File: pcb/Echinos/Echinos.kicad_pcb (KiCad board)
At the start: 2 copper layers, 167 x 135.4 mm, 88 parts, among them J1 Conn_01x06_Socket, J2 Conn_01x06_Socket, J3 Conn_01x06_Socket, J5 SATA-7p, SW1 Reset, SW111 SW_Push, SW112 SW_Push, SW113 SW_Push, SW114 SW_Push, SW115 SW_Push, SW122 SW_Push, SW123 SW_Push, SW124 SW_Push, SW125 SW_Push, SW131 SW_Push, SW132 SW_Push, SW133 SW_Push, SW134 SW_Push, SW135 SW_Push, SW141 SW_Push, SW142 SW_Push, SW143 SW_Push, SW144 SW_Push, SW145 SW_Push, SW151 SW_Push, SW152 SW_Push, SW153 SW_Push, SW154 SW_Push, SW155 SW_Push, U1 Helios, U7 SRV05-4

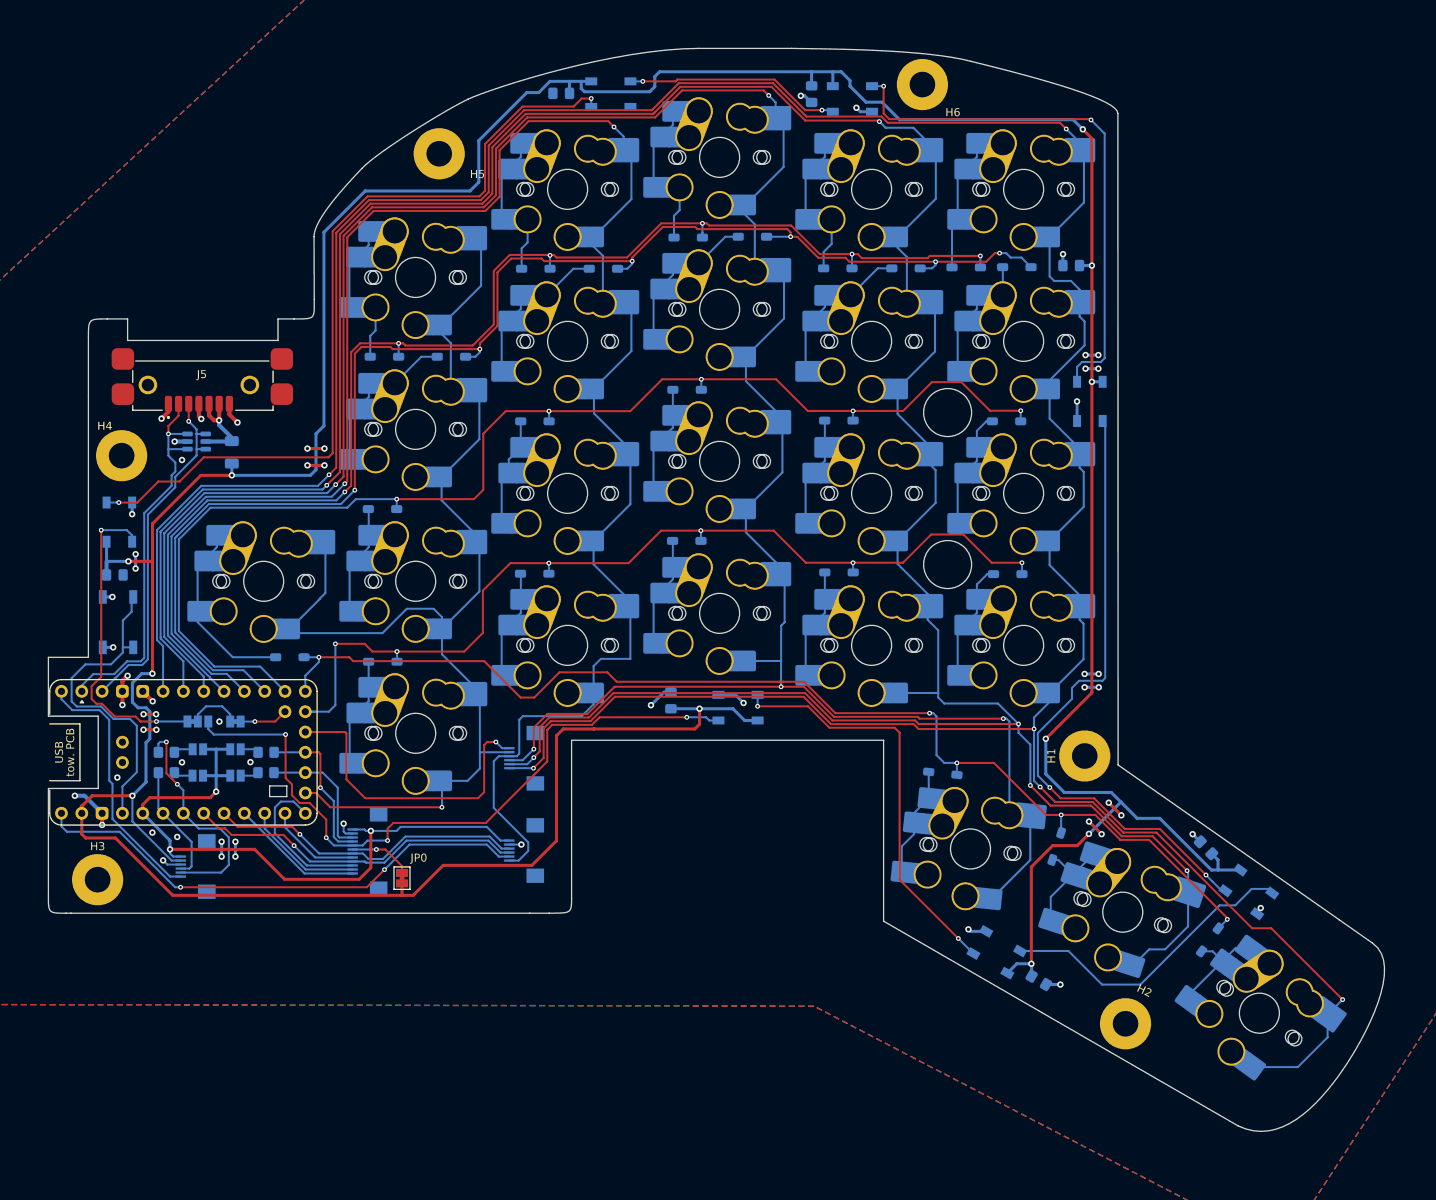
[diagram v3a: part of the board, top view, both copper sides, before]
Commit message: [PCB] - Save last state with Helios MCU board. Add multiple choices for split communication. Also fix SATA footprint and rework board (helios) holes to be smaller (0.9 --> 0.825) to be able to use spring loaded pins. Currently supported split communication are:   - SATA (data)   - USB-B (micro)   - Direct wires to whatever using 2.0 pitch header
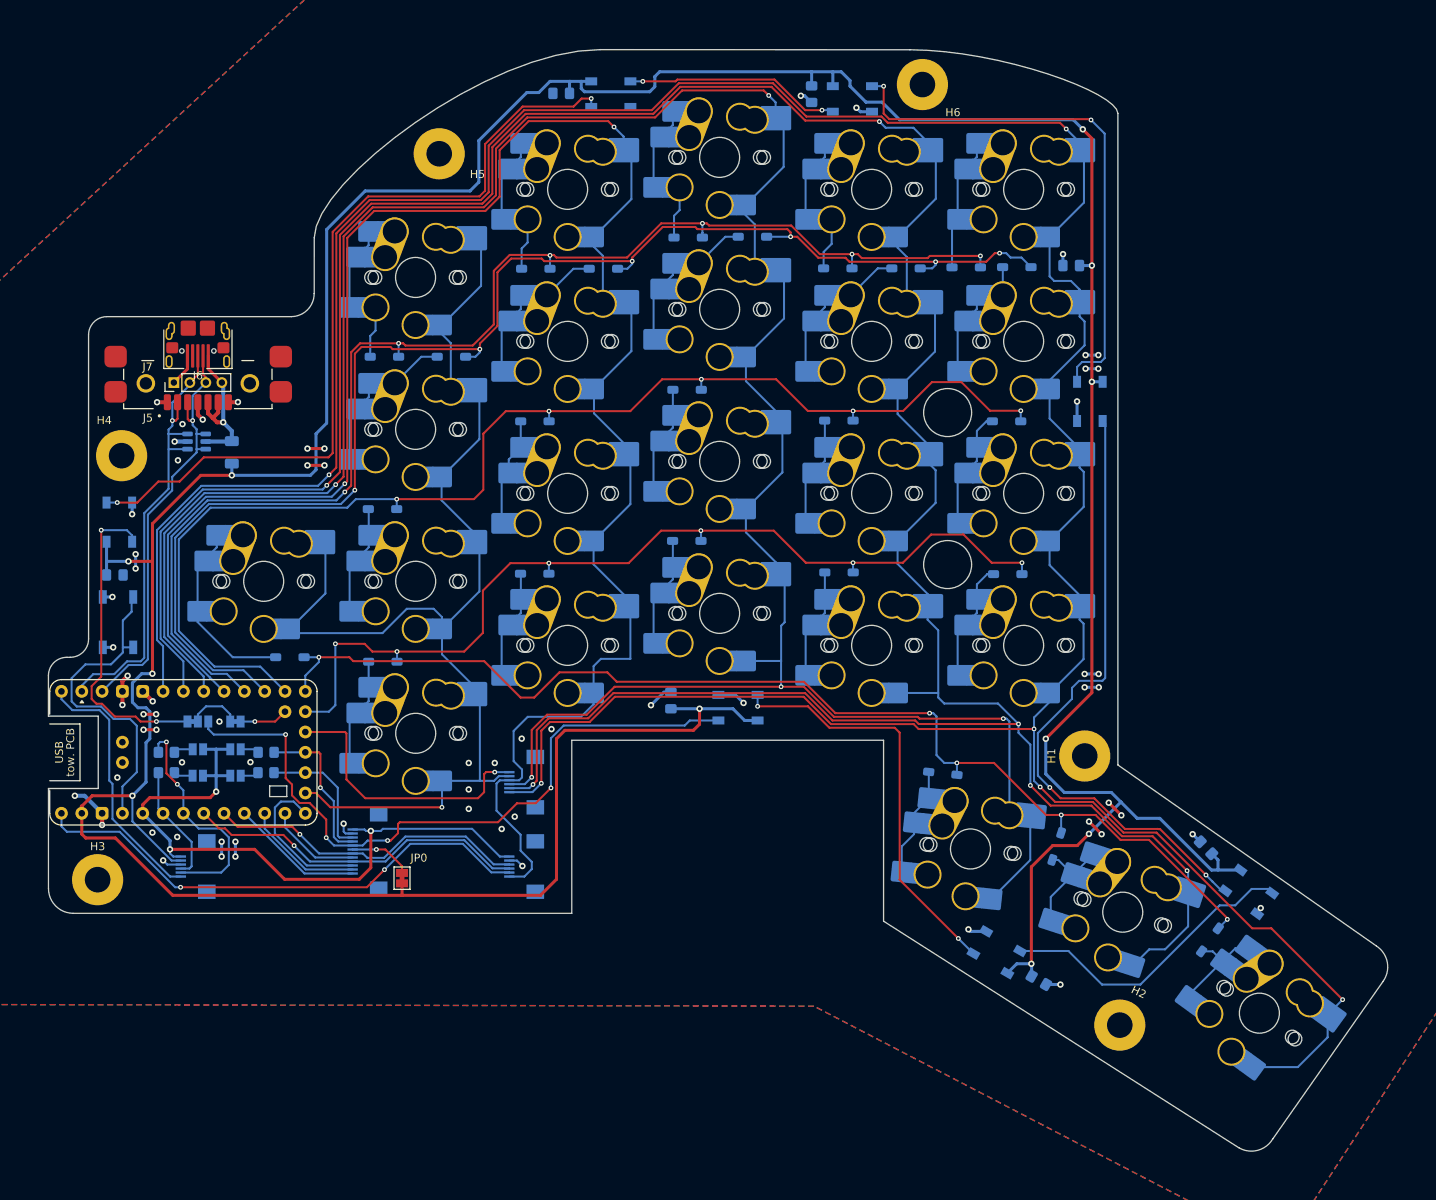
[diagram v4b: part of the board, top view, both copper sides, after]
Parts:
- added J6: USB_B_Micro, Echinos:USB_Micro-B_type5_Amphenol_Horizontal, F.Cu at (64.8, 82.9)
- added J7: Conn_01x04_Socket, Connector_PinHeader_2.00mm:PinHeader_1x04_P2.00mm_Vertical, F.Cu at (61.8, 88.6)
- moved J1 2.99 mm to (105.6, 138.5)
- moved J2 2.00 mm to (105.6, 149.1)
- moved H2 0.74 mm to (180.0, 168.9)
- moved J5 0.66 mm to (64.8, 88.7)
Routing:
- net VBUS_split: track 11.6 -> 21.2 mm
- net RX: track 44.5 -> 54.0 mm
- net TX: track 49.2 -> 58.3 mm
- net row6: track 39.0 -> 35.0 mm
- net col4: track 381.1 -> 384.2 mm
- net col3: track 328.1 -> 331.2 mm
- net col2: track 242.8 -> 245.8 mm
- net col5: track 416.6 -> 419.4 mm
- net GND: track 75.5 -> 78.0 mm, vias 58 -> 67
- net row2: track 119.6 -> 118.4 mm
- net col1: track 143.2 -> 144.3 mm
- net row7: track 63.6 -> 64.5 mm
- net +5V: track 506.1 -> 507.0 mm
- net rgb_out: track 85.9 -> 86.7 mm
- net adc_1: track 42.5 -> 43.3 mm
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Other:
- board size 167 x 135.4 mm -> 167.4 x 137.7 mm

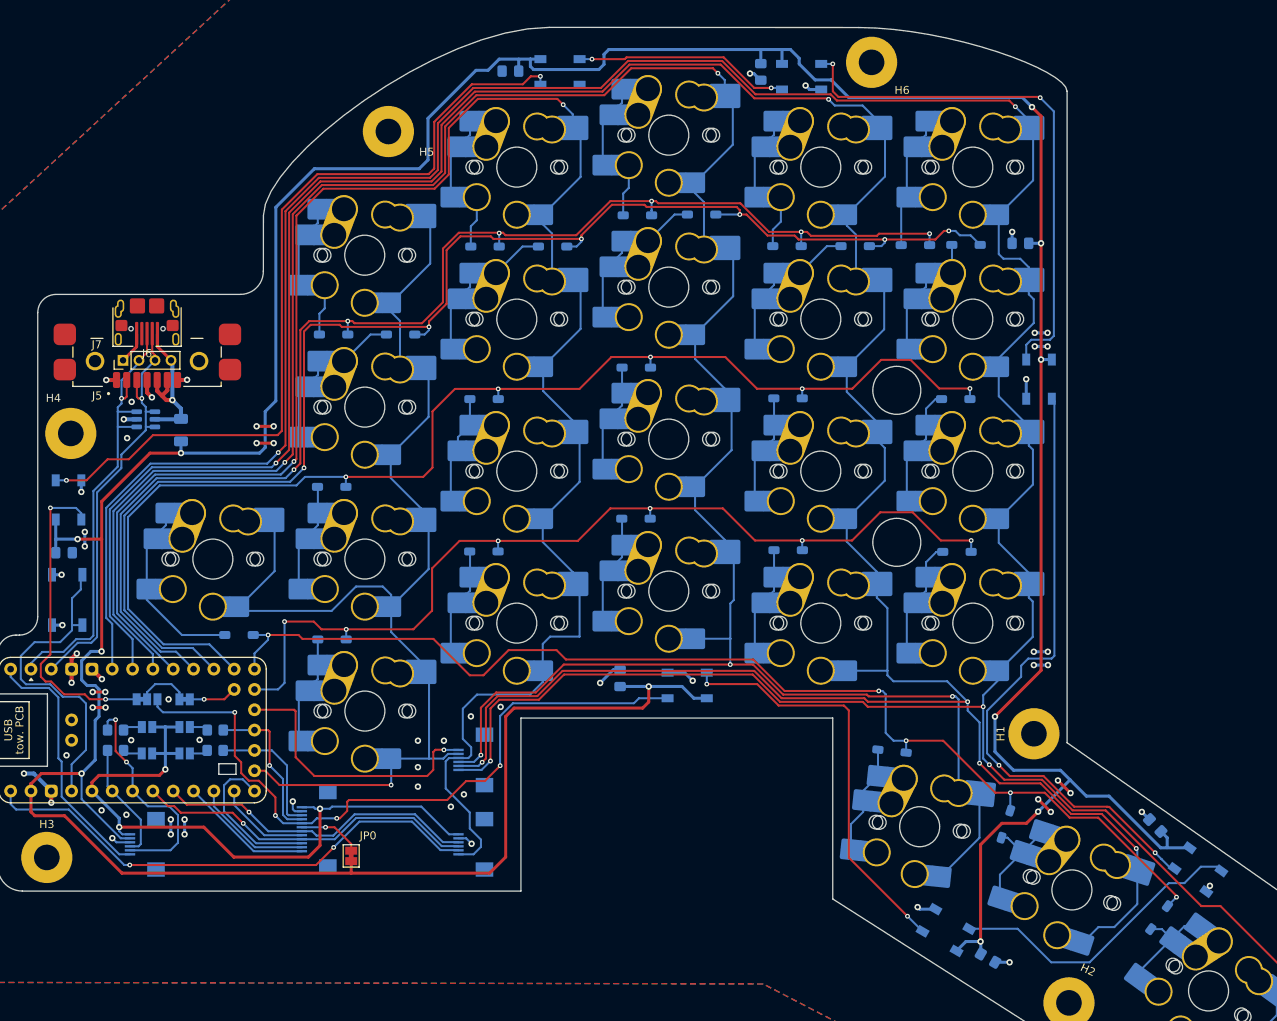
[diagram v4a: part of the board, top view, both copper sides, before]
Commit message: [PCB] - Save last state with Helios MCU board.   - Fix LCSC part numbers (C11, F2)   - Fix pad numbering for SK6812 to match footprint and update PCB traces   - Use another LCSC part for LEDs that is available for economic assembly   - Remove jumpers from BOM (remove warning in JLCPCB)   - Add 180° rotation to FPCs (J1, J2, J3) to match selected part in JLCPCB manufacturing   - Add 180° rotation to LEDs to match selected part in JLCPCB manufacturing
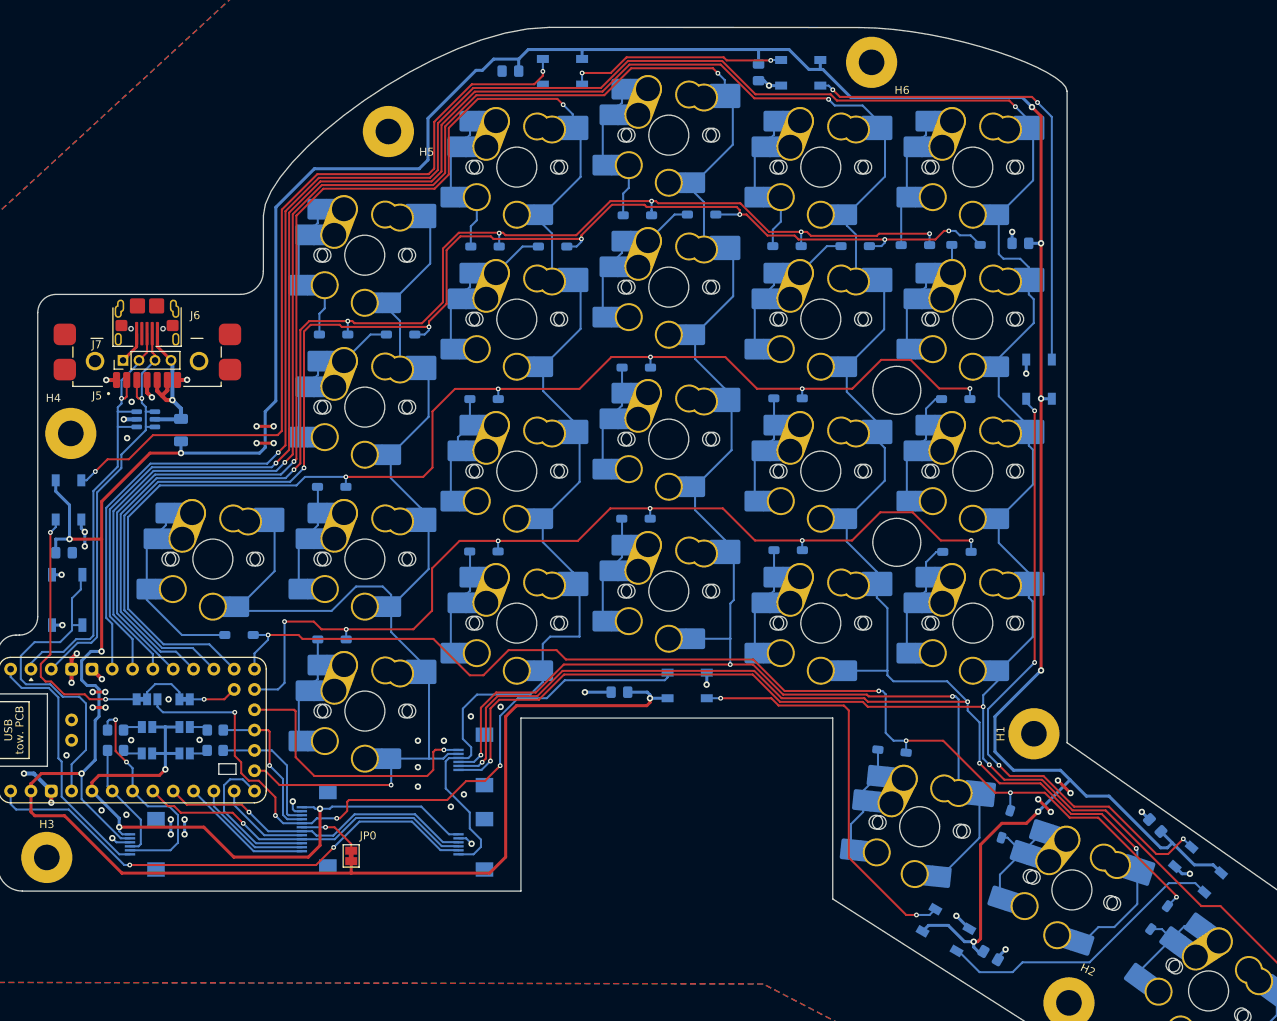
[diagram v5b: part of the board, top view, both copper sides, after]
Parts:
- C17: renamed from C11; value 1µ -> 100nF
- J6: footprint Echinos:USB_Micro-B_type5_Amphenol_Horizontal -> Echinos:USB_Micro-B_Amphenol_type5_micro23_Horizontal
- moved C17 1.74 mm to (123.8, 130.0), turned to 180 degrees
- moved D13 0.50 mm to (146.5, 52.6), turned to 0 degrees
- moved C16 0.46 mm to (170.2, 163.0)
- moved D12 0.31 mm to (116.7, 52.5), turned to 0 degrees
- moved C13 0.29 mm to (141.2, 52.6)
- turned D11 to 90 degrees
- turned D14 to -90 degrees
- turned D15 to -41 degrees
- turned D16 to 150 degrees
- turned D17 to 180 degrees
- renumbered C12 to C11, C13 to C12, C14 to C13, C15 to C14, C16 to C15, C17 to C16
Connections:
- D11 pad 1: Net-(D11-DOUT) -> GND
- D11 pad 2: GND -> /Backlight/backlight_in
- D11 pad 3: /Backlight/backlight_in -> +5V
- D11 pad 4: +5V -> Net-(D11-DOUT)
- D12 pad 1: Net-(D12-DOUT) -> GND
- D12 pad 2: GND -> Net-(D11-DOUT)
- D12 pad 3: Net-(D11-DOUT) -> +5V
- D12 pad 4: +5V -> Net-(D12-DOUT)
- D13 pad 1: Net-(D13-DOUT) -> GND
- D13 pad 2: GND -> Net-(D12-DOUT)
- D13 pad 3: Net-(D12-DOUT) -> +5V
- D13 pad 4: +5V -> Net-(D13-DOUT)
- D14 pad 1: Net-(D14-DOUT) -> GND
- D14 pad 2: GND -> Net-(D13-DOUT)
- D14 pad 3: Net-(D13-DOUT) -> +5V
- D14 pad 4: +5V -> Net-(D14-DOUT)
- D15 pad 1: Net-(D15-DOUT) -> GND
- D15 pad 2: GND -> Net-(D14-DOUT)
- D15 pad 3: Net-(D14-DOUT) -> +5V
- D15 pad 4: +5V -> Net-(D15-DOUT)
- D16 pad 1: Net-(D16-DOUT) -> GND
- D16 pad 2: GND -> Net-(D15-DOUT)
- D16 pad 3: Net-(D15-DOUT) -> +5V
- D16 pad 4: +5V -> Net-(D16-DOUT)
- D17 pad 1: rgb_out -> GND
- D17 pad 2: GND -> Net-(D16-DOUT)
- D17 pad 3: Net-(D16-DOUT) -> +5V
- D17 pad 4: +5V -> rgb_out
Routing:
- net GND: track 78.0 -> 69.3 mm, vias 67 -> 57
- net Net-(D13-DOUT): track 67.4 -> 60.9 mm
- net /Backlight/backlight_in: track 39.7 -> 33.6 mm
- net +5V: track 507.0 -> 512.7 mm
- net Net-(D11-DOUT): track 102.2 -> 100.3 mm
- net rgb_out: track 86.7 -> 88.4 mm
- net Net-(D15-DOUT): track 38.4 -> 37.2 mm
- net Net-(D16-DOUT): track 52.0 -> 50.9 mm
- net Net-(D14-DOUT): track 79.1 -> 79.2 mm, vias 2 -> 4
